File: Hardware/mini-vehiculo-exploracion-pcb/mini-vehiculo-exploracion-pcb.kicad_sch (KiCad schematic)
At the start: 1 part, among them U1 ESP32-S3-WROOM-1-N8R8

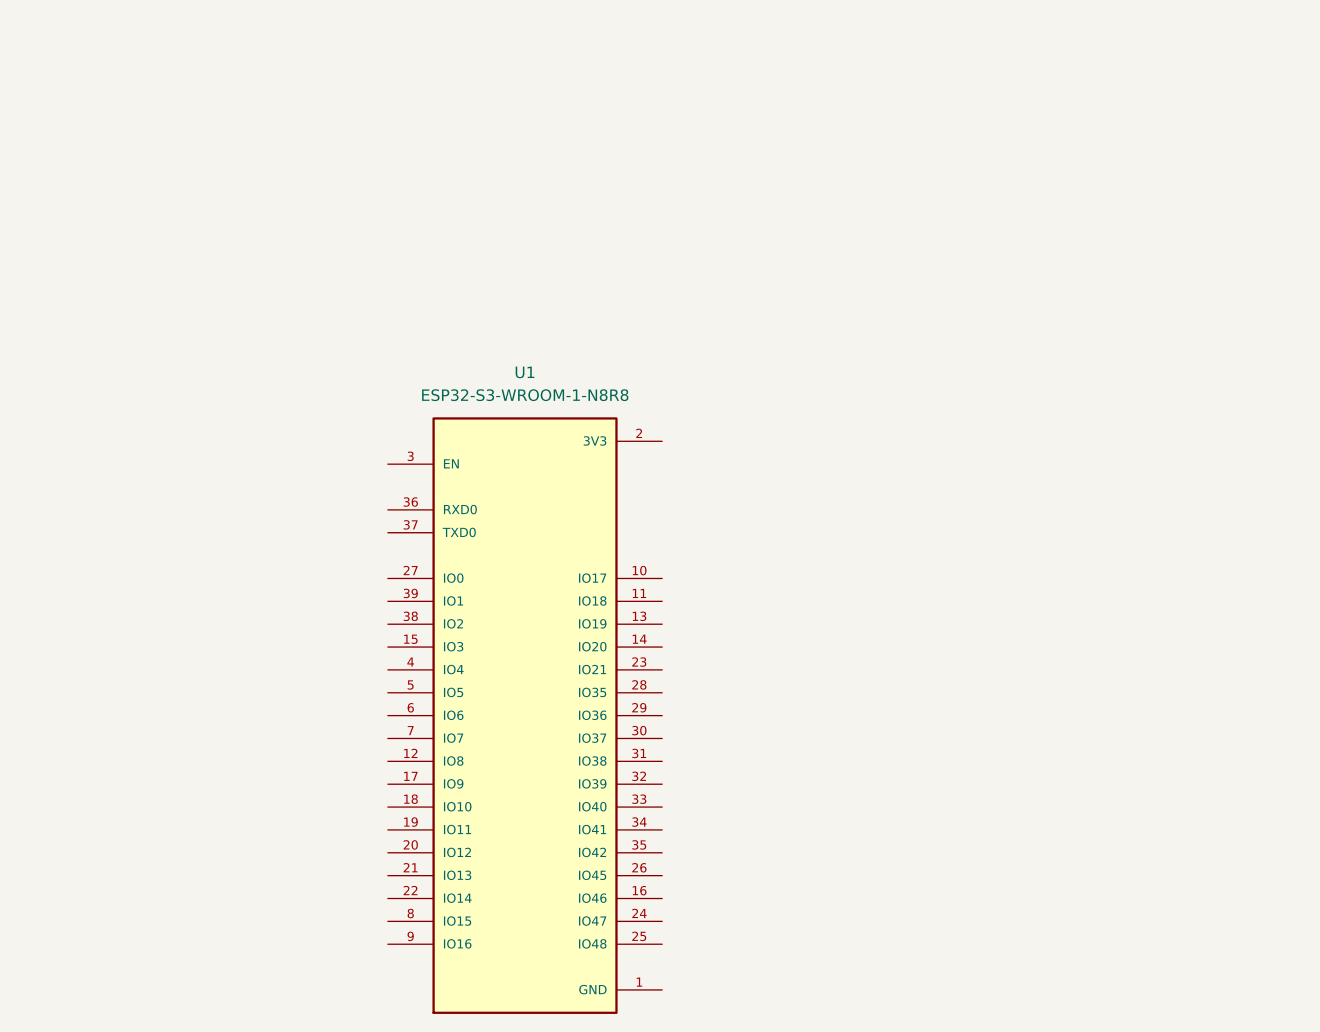
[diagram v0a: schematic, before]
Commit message: Add BNO086 initial
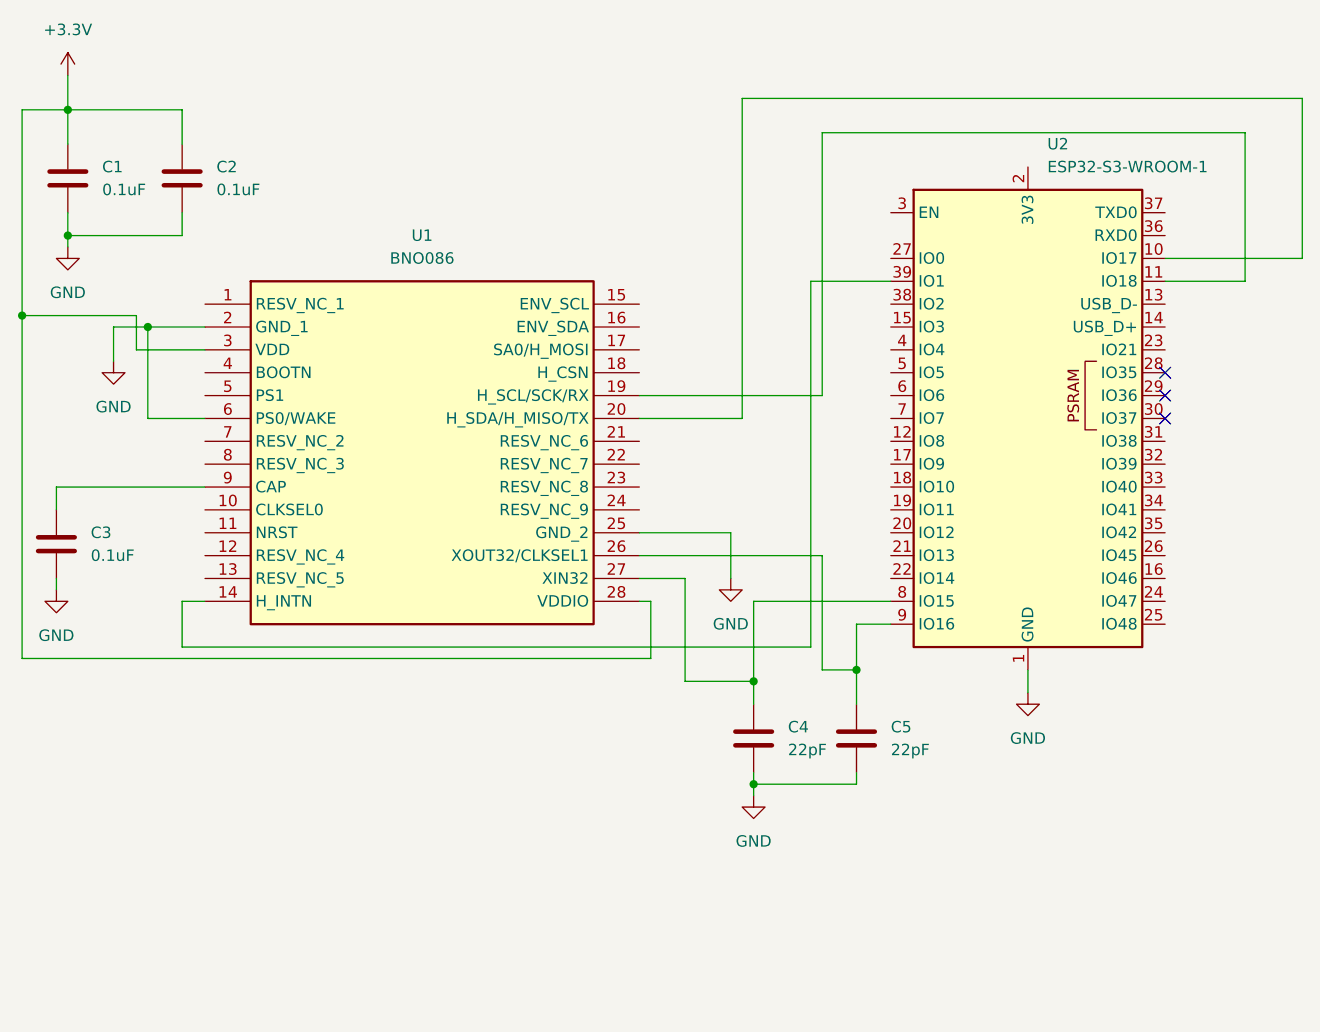
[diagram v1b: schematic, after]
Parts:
- removed U1: ESP32-S3-WROOM-1-N8R8, ESP32-S3-WROOM-1-N8R8:XCVR_ESP32S3WROOM1N8R8, symbol ESP32-S3-WROOM-1-N8R8:ESP32-S3-WROOM-1-N8R8
- added C1, C2, C3: 0.1uF, symbol Device:C
- added C4, C5: 22pF, symbol Device:C
- added U1: BNO086, BNO086, symbol BNO086:BNO086
- added U2: ESP32-S3-WROOM-1, RF_Module:ESP32-S3-WROOM-1, symbol RF_Module:ESP32-S3-WROOM-1
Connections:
- net GND: now also C1.2, C2.2, C3.2, C4.2, C5.2, U1.2 (GND_1), U1.25 (GND_2), U1.6 (PS0/WAKE), U2.1 (GND), U2.40 (GND), U2.41 (GND)
- new net: C5.1, U1.26 (XOUT32/CLKSEL1), U2.9 (IO16)
- new net: U1.20 (H_SDA/H_MISO/TX), U2.10 (IO17)
- new net: U1.19 (H_SCL/SCK/RX), U2.11 (IO18)
- new net: U1.14 (H_INTN), U2.39 (IO1)
- new net: C4.1, U1.27 (XIN32), U2.8 (IO15)
- new net: C3.1, U1.9 (CAP)
- new net +3.3V: C1.1, C2.1, U1.28 (VDDIO), U1.3 (VDD)
- no-connect marks 0 -> 3

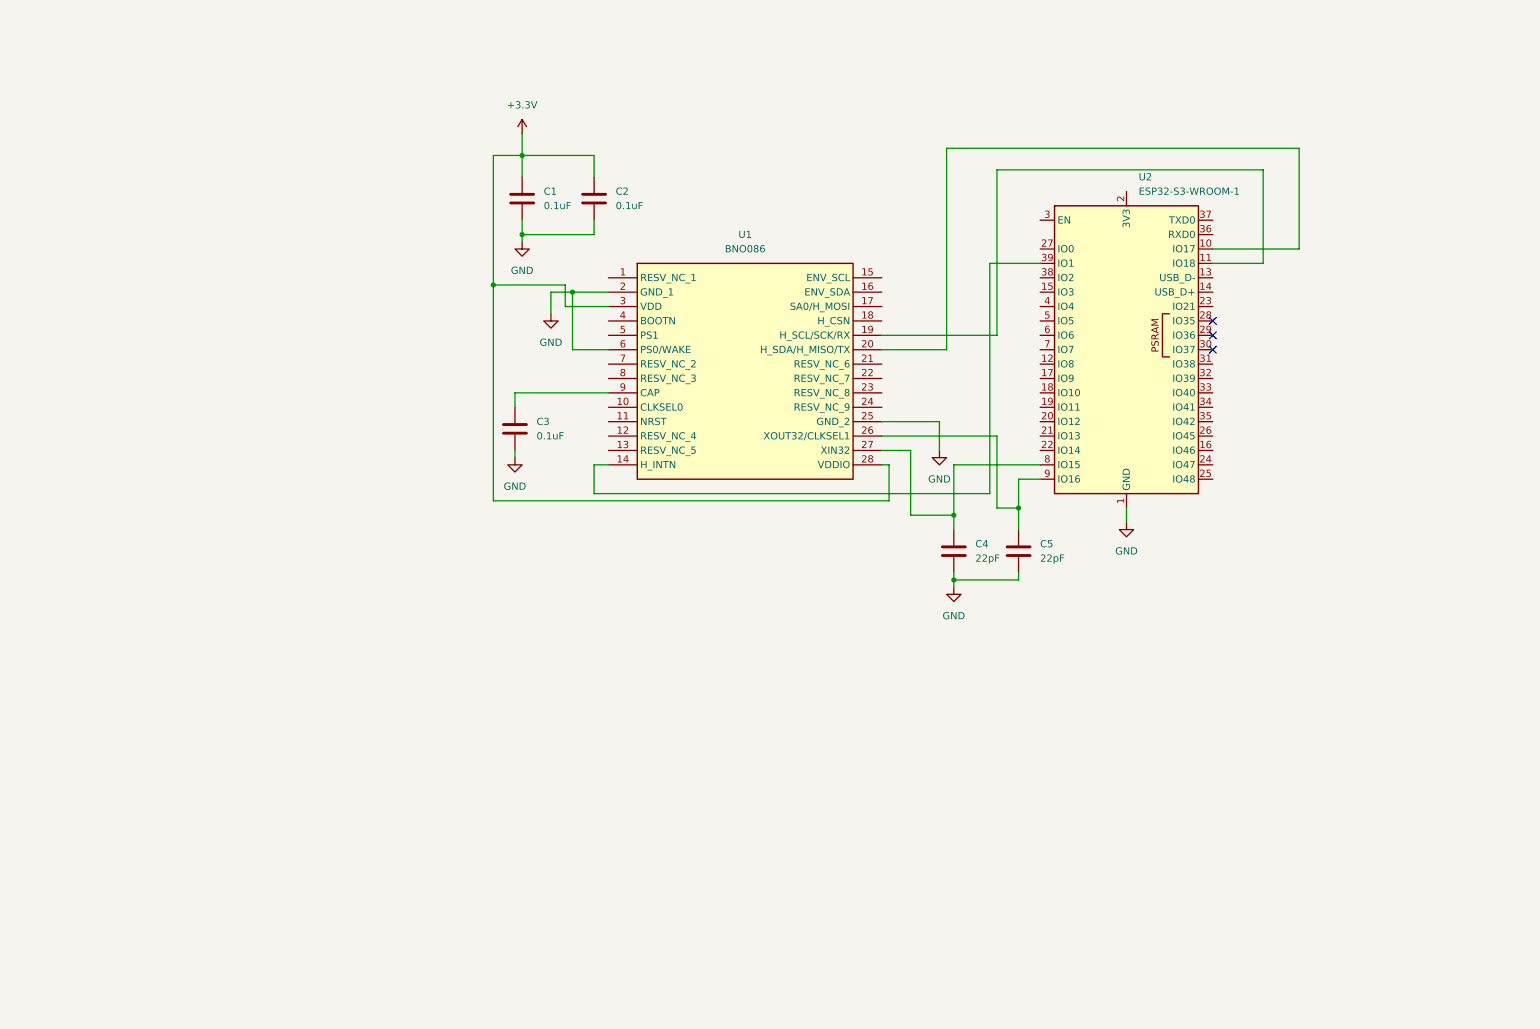
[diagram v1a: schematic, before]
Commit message: Adicion de los drivers para control de motores
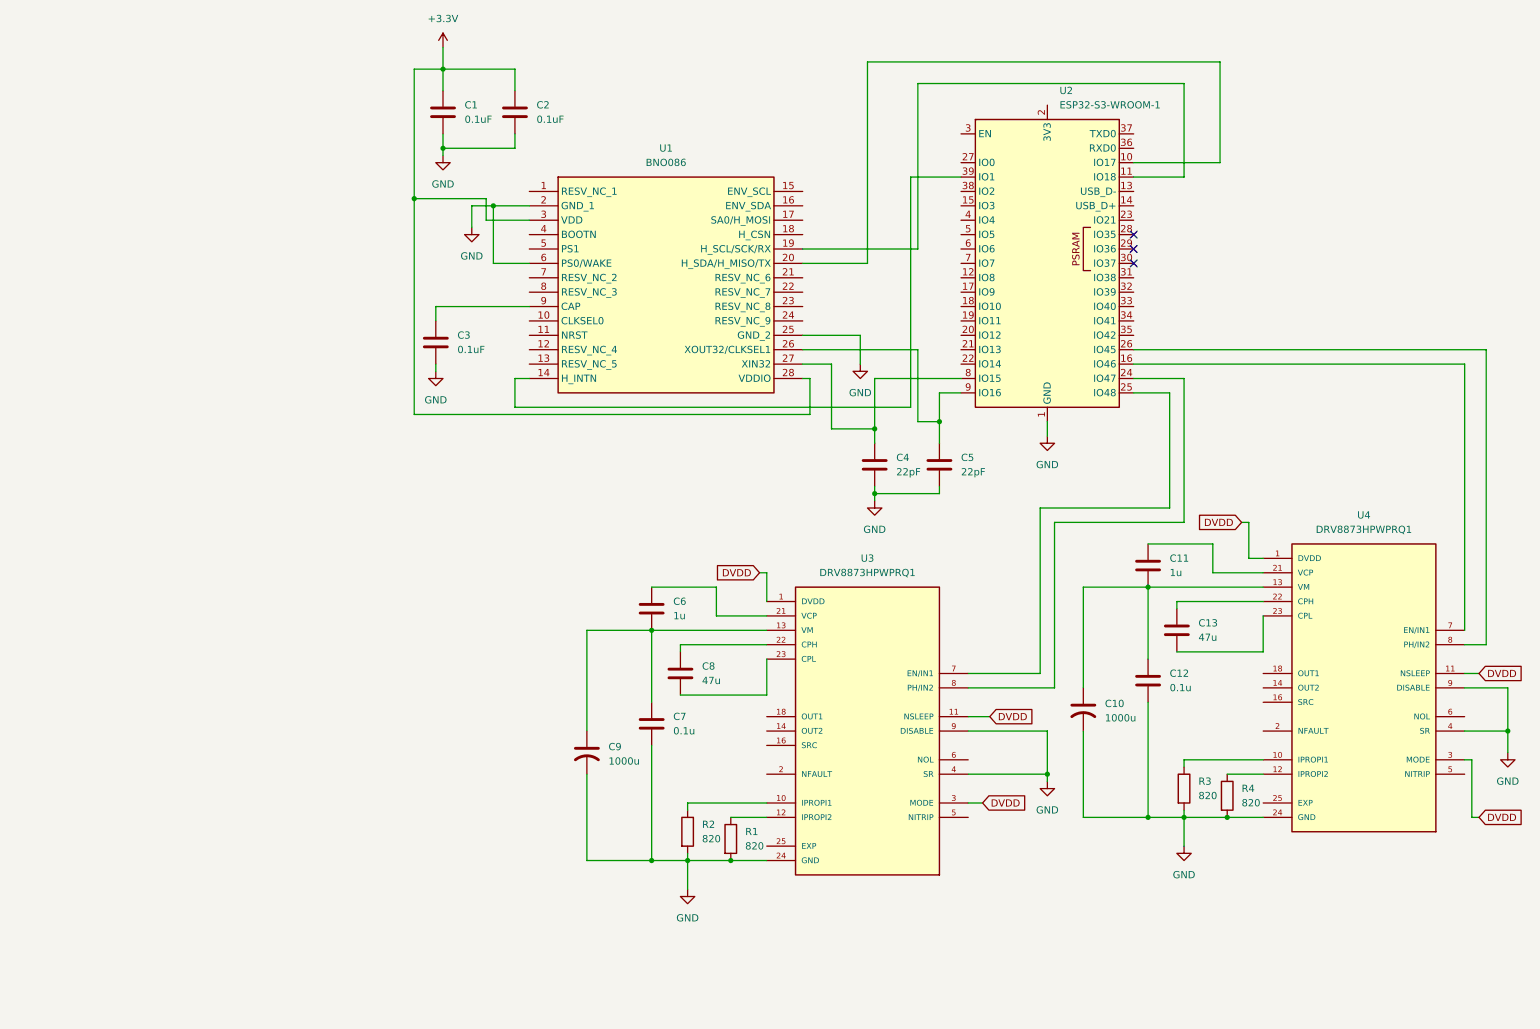
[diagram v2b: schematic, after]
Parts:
- added C10, C9: 1000u, symbol Device:C_US
- added C11, C6: 1u, symbol Device:C
- added C12, C7: 0.1u, symbol Device:C
- added C13, C8: 47u, symbol Device:C
- added R1, R2, R3, R4: 820, symbol Device:R
- added U3, U4: DRV8873HPWPRQ1, DRV8873HPWPRQ1:SOP65P640X120-25N, symbol DRV8873HPWPRQ1:DRV8873HPWPRQ1
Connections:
- net GND: now also C10.2, C12.2, C7.2, C9.2, R1.2, R2.2, R3.2, R4.2, U3.24 (GND), U3.4 (SR), U3.9 (DISABLE), U4.24 (GND), U4.4 (SR), U4.9 (DISABLE)
- net at U2.16 (IO46): now also U4.7 (EN/IN1)
- net at U2.24 (IO47): now also U3.8 (PH/IN2)
- net at U2.25 (IO48): now also U3.7 (EN/IN1)
- net at U2.26 (IO45): now also U4.8 (PH/IN2)
- new net: R2.1, U3.10 (IPROPI1)
- new net: C11.1, U4.21 (VCP)
- new net: R4.1, U4.12 (IPROPI2)
- new net: R1.1, U3.12 (IPROPI2)
- new net: R3.1, U4.10 (IPROPI1)
- new net: U3.14 (OUT2), U3.15 (OUT2)
- new net: U3.16 (SRC), U3.17 (SRC)
- new net: U3.18 (OUT1), U3.19 (OUT1)
- new net: C6.1, U3.21 (VCP)
- new net: C8.1, U3.22 (CPH)
- new net: C8.2, U3.23 (CPL)
- new net: U3.25 (EXP), U3.P1 (EXP), U3.P10 (EXP), U3.P11 (EXP), U3.P12 (EXP), U3.P13 (EXP), U3.P14 (EXP), U3.P15 (EXP), U3.P16 (EXP), U3.P17 (EXP), U3.P18 (EXP), U3.P2 (EXP), U3.P3 (EXP), U3.P4 (EXP), U3.P5 (EXP), U3.P6 (EXP), U3.P7 (EXP), U3.P8 (EXP), U3.P9 (EXP)
- new net: U4.14 (OUT2), U4.15 (OUT2)
- new net: U4.16 (SRC), U4.17 (SRC)
- new net: U4.18 (OUT1), U4.19 (OUT1)
- new net: C13.1, U4.22 (CPH)
- new net: C13.2, U4.23 (CPL)
- new net: U4.25 (EXP), U4.P1 (EXP), U4.P10 (EXP), U4.P11 (EXP), U4.P12 (EXP), U4.P13 (EXP), U4.P14 (EXP), U4.P15 (EXP), U4.P16 (EXP), U4.P17 (EXP), U4.P18 (EXP), U4.P2 (EXP), U4.P3 (EXP), U4.P4 (EXP), U4.P5 (EXP), U4.P6 (EXP), U4.P7 (EXP), U4.P8 (EXP), U4.P9 (EXP)
- new net DVDD: U3.1 (DVDD), U3.11 (NSLEEP), U3.3 (MODE), U4.1 (DVDD), U4.11 (NSLEEP), U4.3 (MODE)
- new net VM: C10.1, C11.2, C12.1, C6.2, C7.1, C9.1, U3.13 (VM), U3.20 (VM), U4.13 (VM), U4.20 (VM)
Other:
- moved on the sheet: C1, C2, C3, C4, C5, U1, U2

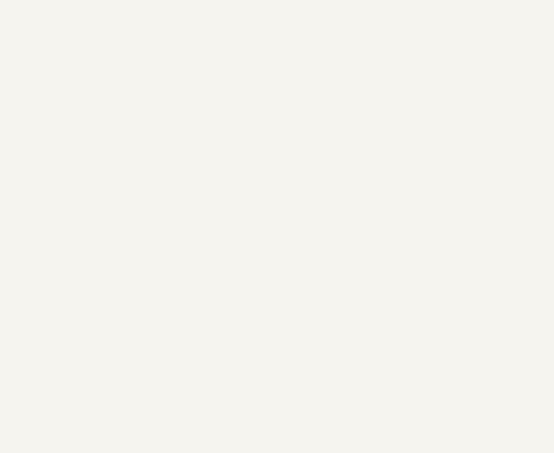
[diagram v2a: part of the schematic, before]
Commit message: Add arducam library
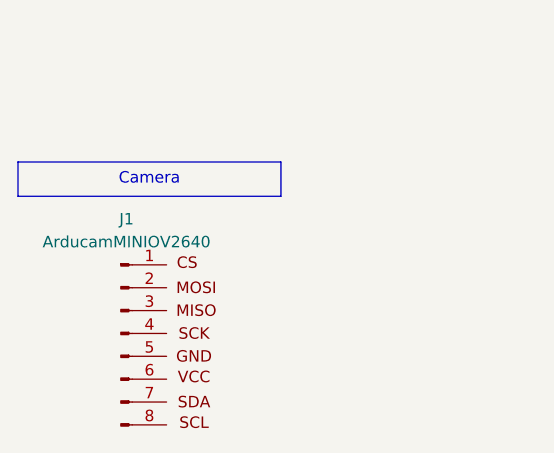
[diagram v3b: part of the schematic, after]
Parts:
- added J1: ArducamMINIOV2640, ArducamMINIOV2640:ArducamMINIOV2640, symbol ArducamMINIOV2640:ArducamMINIOV2640
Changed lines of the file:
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@@
 	(generator_version "9.0")
 	(paper "A4")
+	(text_box "Camera"
+		(exclude_from_sim no)
+		(at 17.78 157.48 0)
+		(size 29.21 3.81)
+		(margins 0.9525 0.9525 0.9525 0.9525)
+		(stroke
+			(width 0)
+			(type solid)
+		)
+		(fill
+			(type none)
+		)
+		(effects
+			(font
+				(size 1.27 1.27)
+			)
+			(justify top)
+		)
+	)
 	(junction
 		(at 170.18 83.82)
@@
 					(unit 1)
 				)
+			)
+		)
+	)
+	(symbol
+		(lib_id "ArducamMINIOV2640:ArducamMINIOV2640")
+		(at 29.21 176.53 0)
+		(unit 1)
+		(exclude_from_sim no)
+		(in_bom yes)
+		(on_board yes)
+		(dnp no)
+		(fields_autoplaced yes)
+		(property "Reference" "J1"
+			(at 29.845 163.83 0)
+			(effects
+				(font
+					(size 1.27 1.27)
+				)
+			)
+		)
+		(property "Value" "ArducamMINIOV2640"
+			(at 29.845 166.37 0)
+			(effects
+				(font
+					(size 1.27 1.27)
+				)
+			)
+		)
+		(property "Footprint" "ArducamMINIOV2640:ArducamMINIOV2640"
+			(at 29.21 176.53 0)
+			(effects
+				(font
+					(size 1.27 1.27)
+				)
+				(hide yes)
+			)
+		)
+		(property "Datasheet" "~"
+			(at 29.21 176.53 0)
+			(effects
+				(font
+					(size 1.27 1.27)
+				)
+				(hide yes)
+			)
+		)
+		(property "Description" "Generic connector, single row, 01x08, script generated"
+			(at 29.21 176.53 0)
+			(effects
+				(font
+					(size 1.27 1.27)
+				)
+				(hide yes)
+			)
+		)
+		(pin "3"
+		)
+		(pin "5"
+		)
+		(pin "7"
+		)
+		(pin "1"
+		)
+		(pin "2"
+		)
+		(pin "4"
+		)
+		(pin "6"
+		)
+		(pin "8"
+		)
+		(instances
+			(project ""
+				(path "/3cb3b833-c38f-47b4-b7e9-f0e6337b7613"
+					(reference "J1")
+					(unit 1)
+				)
